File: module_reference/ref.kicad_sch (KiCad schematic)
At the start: 82 parts, among them J201 Conn_01x01, J202 Conn_01x01, J203 Conn_01x01, J204 Conn_01x01, J205 Conn_01x01, J206 Conn_01x01, J207 Conn_01x01, J208 Conn_01x01, Q201 BD135, U201 ADR1000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

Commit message: Rev 0.5 routed
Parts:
- R222, R224: now left out of the parts list
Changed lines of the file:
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@@
   )
   (symbol (lib_id "Device:R") (at 173.99 52.07 90) (unit 1)
-    (in_bom yes) (on_board yes) (fields_autoplaced)
+    (in_bom no) (on_board yes) (fields_autoplaced)
     (property "Reference" "R222" (id 0) (at 173.99 45.72 90))
     (property "Value" "DNP" (id 1) (at 173.99 48.26 90))
@@
   )
   (symbol (lib_id "Device:R") (at 173.99 102.87 90) (unit 1)
-    (in_bom yes) (on_board yes) (fields_autoplaced)
+    (in_bom no) (on_board yes) (fields_autoplaced)
     (property "Reference" "R224" (id 0) (at 173.99 96.52 90))
     (property "Value" "DNP" (id 1) (at 173.99 99.06 90))

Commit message: No longer configured for PRND by default
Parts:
- added J209, J210, J211, J212: Conn_01x01, Connector_Wire:SolderWire-0.1sqmm_1x01_D0.4mm_OD1mm, symbol Connector_Generic:Conn_01x01
- JP202, JP203, JP207, JP208, JP209, JP213, JP216, JP221: value Jumper_2_Bridged -> Jumper_2_Open; footprint Jumper:SolderJumper-2_P1.3mm_Bridged_RoundedPad1.0x1.5mm -> Jumper:SolderJumper-2_P1.3mm_Open_RoundedPad1.0x1.5mm; symbol Jumper:Jumper_2_Bridged -> Jumper:Jumper_2_Open
- JP204, JP205, JP206, JP210, JP211, JP217, JP219: value Jumper_2_Open -> Jumper_2_Bridged; footprint Jumper:SolderJumper-2_P1.3mm_Open_RoundedPad1.0x1.5mm -> Jumper:SolderJumper-2_P1.3mm_Bridged_RoundedPad1.0x1.5mm; symbol Jumper:Jumper_2_Open -> Jumper:Jumper_2_Bridged
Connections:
- net ADR_Pin6: now also J212.1 (Pin_1); no longer RN201.5 (R5.1)
- net ADR_Pin7: now also J209.1 (Pin_1)
- net RN201_Pin15: now also J210.1 (Pin_1)
- new net RN201_Pin5: J211.1 (Pin_1), RN201.5 (R5.1)
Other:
- moved on the sheet: J202, J204, J205, J207, JP203, JP204, JP205, JP206, JP209, JP210, JP216, JP217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

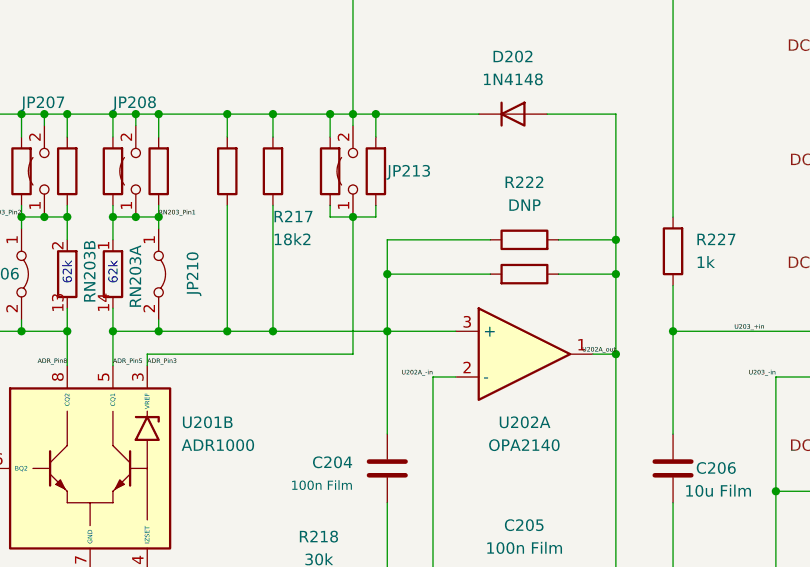
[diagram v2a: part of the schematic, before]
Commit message: New backplane, Reference Rev 0.6 with heated resistor network support
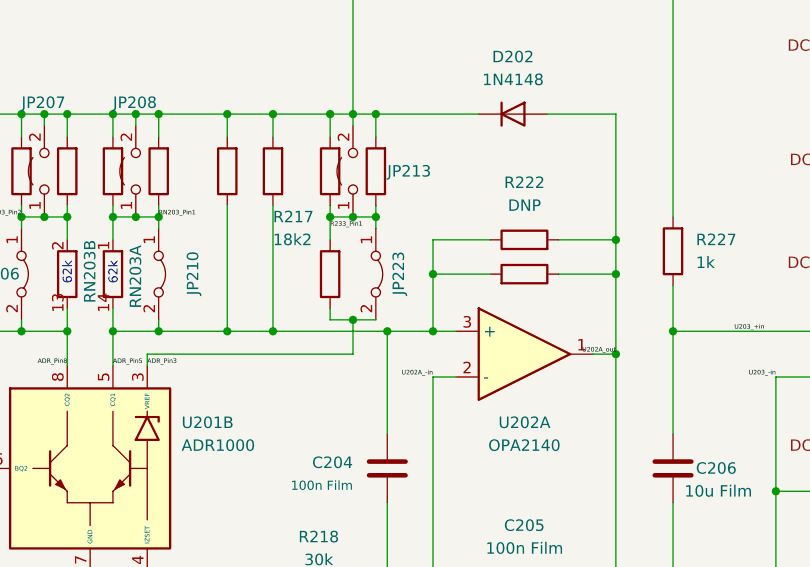
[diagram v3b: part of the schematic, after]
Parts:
- added JP223: Jumper_2_Bridged, Jumper:SolderJumper-2_P1.3mm_Bridged_RoundedPad1.0x1.5mm, symbol Jumper:Jumper_2_Bridged
- added R233: 0, Resistor_THT:R_Axial_DIN0204_L3.6mm_D1.6mm_P7.62mm_Horizontal, symbol Device:R
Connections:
- net ADR_Pin3: now also JP223.2 (B), R233.1; no longer JP213.1 (A), R219.1, R220.1
- new net R233_Pin1: JP213.1 (A), JP223.1 (A), R219.1, R220.1, R233.2
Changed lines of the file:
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@@
   (title_block
     (title "Reference and 10V buffer circuit")
-    (date "2022-05-23")
-    (rev "0.5")
+    (date "2022-08-15")
+    (rev "0.6")
     (company "RPG")
     (comment 1 "All resistors 0.1% MF unless otherwise noted")
@@
   (junction (at 71.12 179.07) (diameter 0) (color 0 0 0 0)
   )
+  (junction (at 163.83 62.23) (diameter 0) (color 0 0 0 0)
+  )
   (junction (at 71.12 191.77) (diameter 0) (color 0 0 0 0)
   )
@@
   (junction (at 241.3 133.35) (diameter 0) (color 0 0 0 0)
   )
-  (junction (at 158.75 55.88) (diameter 0) (color 0 0 0 0)
-  )
   (junction (at 265.43 147.32) (diameter 0) (color 0 0 0 0)
   )
@@
   (junction (at 62.23 179.07) (diameter 0) (color 0 0 0 0)
   )
+  (junction (at 152.4 49.53) (diameter 0) (color 0 0 0 0)
+  )
   (junction (at 163.83 102.87) (diameter 0) (color 0 0 0 0)
   )
@@
   (junction (at 176.53 143.51) (diameter 0) (color 0 0 0 0)
   )
+  (junction (at 157.48 49.53) (diameter 0) (color 0 0 0 0)
+  )
   (junction (at 140.97 62.23) (diameter 0) (color 0 0 0 0)
   )
@@
   (junction (at 233.68 90.17) (diameter 0) (color 0 0 0 0)
   )
+  (junction (at 163.83 55.88) (diameter 0) (color 0 0 0 0)
+  )
   (junction (at 201.93 102.87) (diameter 0) (color 0 0 0 0)
   )
@@
   (junction (at 129.54 114.3) (diameter 0) (color 0 0 0 0)
   )
+  (junction (at 154.94 60.96) (diameter 0) (color 0 0 0 0)
+  )
   (junction (at 232.41 133.35) (diameter 0) (color 0 0 0 0)
   )
@@
   (no_connect (at 223.52 72.39))
   (no_connect (at 220.98 72.39))
+  (wire (pts (xy 157.48 50.8) (xy 157.48 49.53))
+    (stroke (width 0) (type default) (color 0 0 0 0))
+  )
   (wire (pts (xy 218.44 72.39) (xy 218.44 74.93))
     (stroke (width 0) (type default) (color 0 0 0 0))
@@
     (stroke (width 0) (type default) (color 0 0 0 0))
   )
-  (wire (pts (xy 158.75 62.23) (xy 166.37 62.23))
-    (stroke (width 0) (type default) (color 0 0 0 0))
-  )
   (wire (pts (xy 154.94 91.44) (xy 163.83 91.44))
     (stroke (width 0) (type default) (color 0 0 0 0))
@@
     (stroke (width 0) (type default) (color 0 0 0 0))
   )
-  (wire (pts (xy 158.75 55.88) (xy 170.18 55.88))
-    (stroke (width 0) (type default) (color 0 0 0 0))
-  )
   (wire (pts (xy 231.14 64.77) (xy 238.76 64.77))
     (stroke (width 0) (type default) (color 0 0 0 0))
@@
     (stroke (width 0) (type default) (color 0 0 0 0))
   )
+  (wire (pts (xy 163.83 55.88) (xy 170.18 55.88))
+    (stroke (width 0) (type default) (color 0 0 0 0))
+  )
   (wire (pts (xy 93.98 62.23) (xy 118.11 62.23))
     (stroke (width 0) (type default) (color 0 0 0 0))
@@
     (stroke (width 0) (type default) (color 0 0 0 0))
   )
+  (wire (pts (xy 163.83 62.23) (xy 166.37 62.23))
+    (stroke (width 0) (type default) (color 0 0 0 0))
+  )
   (wire (pts (xy 177.8 106.68) (xy 184.15 106.68))
     (stroke (width 0) (type default) (color 0 0 0 0))
@@
     (stroke (width 0) (type default) (color 0 0 0 0))
   )
+  (wire (pts (xy 157.48 60.96) (xy 154.94 60.96))
+    (stroke (width 0) (type default) (color 0 0 0 0))
+  )
   (wire (pts (xy 265.43 133.35) (xy 274.32 133.35))
     (stroke (width 0) (type default) (color 0 0 0 0))
@@
     (stroke (width 0) (type default) (color 0 0 0 0))
   )
-  (wire (pts (xy 158.75 55.88) (xy 158.75 52.07))
+  (wire (pts (xy 163.83 55.88) (xy 163.83 52.07))
+    (stroke (width 0) (type default) (color 0 0 0 0))
+  )
+  (wire (pts (xy 154.94 60.96) (xy 152.4 60.96))
     (stroke (width 0) (type default) (color 0 0 0 0))
   )
@@
     (stroke (width 0) (type default) (color 0 0 0 0))
   )
+  (wire (pts (xy 154.94 64.77) (xy 154.94 60.96))
+    (stroke (width 0) (type default) (color 0 0 0 0))
+  )
   (wire (pts (xy 138.43 153.67) (xy 138.43 158.75))
     (stroke (width 0) (type default) (color 0 0 0 0))
@@
     (stroke (width 0) (type default) (color 0 0 0 0))
   )
+  (wire (pts (xy 152.4 60.96) (xy 152.4 59.69))
+    (stroke (width 0) (type default) (color 0 0 0 0))
+  )
   (wire (pts (xy 40.64 154.94) (xy 45.72 154.94))
     (stroke (width 0) (type default) (color 0 0 0 0))
@@
     (stroke (width 0) (type default) (color 0 0 0 0))
   )
+  (wire (pts (xy 152.4 52.07) (xy 152.4 49.53))
+    (stroke (width 0) (type default) (color 0 0 0 0))
+  )
   (wire (pts (xy 118.11 62.23) (xy 123.19 62.23))
     (stroke (width 0) (type default) (color 0 0 0 0))
@@
     (stroke (width 0) (type default) (color 0 0 0 0))
   )
-  (wire (pts (xy 158.75 62.23) (xy 158.75 55.88))
+  (wire (pts (xy 163.83 62.23) (xy 163.83 55.88))
     (stroke (width 0) (type default) (color 0 0 0 0))
   )
@@
     (stroke (width 0) (type default) (color 0 0 0 0))
   )
+  (wire (pts (xy 158.75 62.23) (xy 163.83 62.23))
+    (stroke (width 0) (type default) (color 0 0 0 0))
+  )
   (wire (pts (xy 120.65 38.1) (xy 123.19 38.1))
     (stroke (width 0) (type default) (color 0 0 0 0))
@@
     (stroke (width 0) (type default) (color 0 0 0 0))
   )
-  (wire (pts (xy 154.94 49.53) (xy 154.94 64.77))
-    (stroke (width 0) (type default) (color 0 0 0 0))
-  )
   (wire (pts (xy 85.09 53.34) (xy 93.98 53.34))
     (stroke (width 0) (type default) (color 0 0 0 0))
@@
     (stroke (width 0) (type default) (color 0 0 0 0))
   )
-  (wire (pts (xy 158.75 52.07) (xy 170.18 52.07))
+  (wire (pts (xy 163.83 52.07) (xy 170.18 52.07))
     (stroke (width 0) (type default) (color 0 0 0 0))
   )
@@
     (effects (font (size 1.27 1.27)) (justify left bottom))
   )
+  (label "R233_Pin1" (at 152.4 50.8 0)
+    (effects (font (size 0.5 0.5)) (justify left bottom))
+  )
   (label "RN201_Pin5" (at 54.61 154.94 0)
     (effects (font (size 0.635 0.635)) (justify left bottom))
@@
     (pin "2")
   )
-  (symbol (lib_id "ADRmu_Library:322146") (at 105.41 96.52 180) (unit 4)
+  (symbol (lib_name "322146_4") (lib_id "ADRmu_Library:322146") (at 105.41 96.52 180) (unit 4)
     (in_bom yes) (on_board yes)
     (property "Reference" "RN203" (id 0) (at 102.87 100.33 90)
@@
     (pin "2")
   )
+  (symbol (lib_id "Device:R") (at 152.4 55.88 180) (unit 1)
+    (in_bom no) (on_board yes) (fields_autoplaced)
+    (property "Reference" "R233" (id 0) (at 154.94 54.6099 0)
+      (effects (font (size 1.27 1.27)) (justify right) hide)
+    )
+    (property "Value" "0" (id 1) (at 154.94 57.1499 0)
+      (effects (font (size 1.27 1.27)) (justify right) hide)
+    )
+    (property "Footprint" "Resistor_THT:R_Axial_DIN0204_L3.6mm_D1.6mm_P7.62mm_Horizontal" (id 2) (at 154.178 55.88 90)
+      (effects (font (size 1.27 1.27)) hide)
+    )
+    (property "Datasheet" "~" (id 3) (at 152.4 55.88 0)
+      (effects (font (size 1.27 1.27)) hide)
+    )
+    (pin "1")
+    (pin "2")
+  )
   (symbol (lib_id "Jumper:Jumper_2_Open") (at 201.93 107.95 270) (unit 1)
     (in_bom no) (on_board yes)
@@
     (pin "3")
   )
-  (symbol (lib_id "ADRmu_Library:322146") (at 128.27 55.88 0) (unit 1)
+  (symbol (lib_name "322146_1") (lib_id "ADRmu_Library:322146") (at 128.27 55.88 0) (unit 1)
     (in_bom yes) (on_board yes)
     (property "Reference" "RN203" (id 0) (at 130.81 59.69 90)
@@
     (pin "2")
   )
-  (symbol (lib_id "ADRmu_Library:322146") (at 123.19 55.88 0) (unit 2)
+  (symbol (lib_name "322146_2") (lib_id "ADRmu_Library:322146") (at 123.19 55.88 0) (unit 2)
     (in_bom yes) (on_board yes)
     (property "Reference" "RN203" (id 0) (at 125.73 52.07 90)
@@
     (pin "2")
   )
-  (symbol (lib_id "ADRmu_Library:322146") (at 129.54 96.52 180) (unit 3)
+  (symbol (lib_name "322146_5") (lib_id "ADRmu_Library:322146") (at 129.54 96.52 180) (unit 3)
     (in_bom yes) (on_board yes)
     (property "Reference" "RN203" (id 0) (at 127 100.33 90)
@@
     (pin "2")
   )
-  (symbol (lib_id "ADRmu_Library:322146") (at 105.41 71.12 0) (unit 5)
+  (symbol (lib_name "322146_3") (lib_id "ADRmu_Library:322146") (at 105.41 71.12 0) (unit 5)
     (in_bom yes) (on_board yes)
     (property "Reference" "RN203" (id 0) (at 102.87 71.12 0)
@@
     (pin "2")
   )
-  (symbol (lib_id "ADRmu_Library:322146") (at 217.17 87.63 270) (unit 6)
+  (symbol (lib_name "322146_6") (lib_id "ADRmu_Library:322146") (at 217.17 87.63 270) (unit 6)
     (in_bom yes) (on_board yes)
     (property "Reference" "RN203" (id 0) (at 217.17 85.09 90))
@@
     (pin "9")
   )
+  (symbol (lib_id "Jumper:Jumper_2_Bridged") (at 157.48 55.88 270) (unit 1)
+    (in_bom no) (on_board yes)
+    (property "Reference" "JP223" (id 0) (at 160.02 53.34 0)
+      (effects (font (size 1.27 1.27)) (justify left))
+    )
+    (property "Value" "Jumper_2_Bridged" (id 1) (at 154.94 55.88 0)
+      (effects (font (size 1.27 1.27)) hide)
+    )
+    (property "Footprint" "Jumper:SolderJumper-2_P1.3mm_Bridged_RoundedPad1.0x1.5mm" (id 2) (at 157.48 55.88 0)
+      (effects (font (size 1.27 1.27)) hide)
+    )
+    (property "Datasheet" "~" (id 3) (at 157.48 55.88 0)
+      (effects (font (size 1.27 1.27)) hide)
+    )
+    (pin "1")
+    (pin "2")
+  )
   (symbol (lib_id "Device:R") (at 171.45 137.16 0) (mirror x) (unit 1)

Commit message: Ref module Rev. 0.9
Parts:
- removed C206: 10u Film, Capacitor_THT:C_Rect_L7.2mm_W11.0mm_P5.00mm_FKS2_FKP2_MKS2_MKP2, symbol Device:C
- removed C207: 100n 50V, Capacitor_SMD:C_0805_2012Metric, symbol Device:C
- removed C208: 220n Film, Capacitor_THT:C_Rect_L7.2mm_W3.0mm_P5.00mm_FKS2_FKP2_MKS2_MKP2, symbol Device:C
- removed C209: 1u Film, Capacitor_THT:C_Rect_L4.6mm_W5.5mm_P2.50mm_MKS02_FKP02, symbol Device:C
- removed JP212, JP214, JP215, JP216, JP221: Jumper_2_Open, Jumper:SolderJumper-2_P1.3mm_Open_RoundedPad1.0x1.5mm, symbol Jumper:Jumper_2_Open
- removed JP217, JP219: Jumper_2_Bridged, Jumper:SolderJumper-2_P1.3mm_Bridged_RoundedPad1.0x1.5mm, symbol Jumper:Jumper_2_Bridged
- removed R228, R231: 0, Crystal:Crystal_HC52-U_Vertical, symbol Device:R
- removed R229, R230: 0, Resistor_SMD:R_0805_2012Metric, symbol Device:R
- removed R232: 100, Resistor_SMD:R_0805_2012Metric, symbol Device:R
- removed R233: 0, Resistor_THT:R_Axial_DIN0204_L3.6mm_D1.6mm_P7.62mm_Horizontal, symbol Device:R
- removed RN202: Vishay TDP 10k, Package_DIP:DIP-16_W7.62mm, symbol ADRmu_Library:Vishay TDP
- removed RN203: 322146, Package_DIP:DIP-14_W7.62mm, symbol ADRmu_Library:322146
- removed U203: ADA4523-1, Package_SO:SOIC-8_3.9x4.9mm_P1.27mm, symbol ADRmu_Library:ADA4523-1
- added J214, J215, J216, J217: Conn_01x01, Connector_Wire:SolderWire-0.1sqmm_1x01_D0.4mm_OD1mm, symbol Connector_Generic:Conn_01x01
- added JPB201, JPH201: Jumper_2_Open, Jumper:SolderJumper-2_P1.3mm_Open_RoundedPad1.0x1.5mm, symbol Jumper:Jumper_2_Open
- added R234: 10k, Resistor_SMD:R_0805_2012Metric, symbol Device:R
- added RN203: 322146+1, ADRmu_Library:VPG322146+1, symbol ADRmu_Library:322146+1
- added TP201: TestPoint, TestPoint:TestPoint_THTPad_2.0x2.0mm_Drill1.0mm, symbol Connector:TestPoint
- C201, C202, C203: footprint Capacitor_SMD:C_0805_2012Metric -> Capacitor_SMD:C_0603_1608Metric
- C204, C205: value 100n Film -> 100n 50V; footprint Capacitor_THT:C_Rect_L7.2mm_W2.5mm_P5.00mm_FKS2_FKP2_MKS2_MKP2 -> Capacitor_SMD:C_0603_1608Metric
- J201, J202, J203, J204, J205, J206, J207, J208, J209, J210, J211, J212: now left out of the parts list
- R216, R217: value 18k2 -> DNP
- R221: footprint Crystal:Crystal_HC52-U_Vertical -> Resistor_SMD:R_0805_2012Metric; now in the parts list
- R222, R223, R224, R225, R226: value DNP -> TBD
- R227: value 1k -> TBD; now left out of the parts list
- U202: value OPA2140 -> OPA2172
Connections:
- net U203_+in is gone; now on net U202A_-in: R227.1
- net 7Vref: now also R221.1, J214.1 (Pin_1); no longer R227.2
- net ADR_Pin3: now also RN203.8 (1.1)
- net ADR_Pin4: now also RN203.12 (R3.2)
- net ADR_Pin5: now also R226.1, RN203.14 (1.2)
- net ADR_Pin6: now also J217.1 (Pin_1), R234.2, RN203.11 (R4.2), RN203.11 (R5.2); no longer J212.1 (Pin_1), RN201.6 (R6.1)
- net ADR_Pin7: now also J215.1 (Pin_1), J216.1 (Pin_1), JPB201.2 (B); no longer J209.1 (Pin_1), RN201.10 (R7.2)
- net ADR_Pin8: now also RN203.13 (R2.2)
- net Q201_base: now also TP201.1
- net RN203_Pin1: now also RN203.1 (1.1)
- net RN203_Pin2: now also RN203.2 (R2.1)
- net RN203_Pin3: now also RN203.3 (R3.1)
- net RN203_Pin4: now also RN203.4 (R4.1)
- net RN203_Pin5: now also RN203.5 (R5.1)
- net U202A_out: now also R226.2, R227.2
- net DC_DC_GND renamed GNDf
- net GNDf: now also JPH201.2 (B); no longer D201.1 (K)
- net DC_DC_Vin+ renamed 12Vf
- net 12Vf: now also R221.2
- removed net JP214_Pin2: R221.1, R226.1
- net R206_Pin1 renamed R204_Pin1
- net R233_Pin1 renamed J213_Pin1
- net J213_Pin1: now also RN203.9 (8..2)
- removed net RN202_Pin9: R221.2, R226.2
- new net JPB_Pin1: JPB201.1 (A), R234.1
- new net JPH_Pin1: D201.1 (K), JPH201.1 (A)
- new net RN201_Pin10: J209.1 (Pin_1), RN201.10 (R7.2)
- new net RN201_Pin6: J212.1 (Pin_1), RN201.6 (R6.1)
- no-connect marks 2 -> 0
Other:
- note removed: "10k"
- note removed: "13k"
- note removed: "1k"
- note removed: "20k"
- note removed: "62k"
- note removed: "95R"
- title: Reference and 10V buffer circuit -> Reference circuit
- moved on the sheet: C201, C202, C203, C204, D201, D202, J203, J208, J209, J212, JP201, JP202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

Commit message: asdf
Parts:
- removed JP213: Jumper_2_Open, Jumper:SolderJumper-2_P1.3mm_Open_RoundedPad1.0x1.5mm, symbol Jumper:Jumper_2_Open
- added JP213: Jumper_2_Bridged, Jumper:SolderJumper-2_P1.3mm_Bridged_RoundedPad1.0x1.5mm, symbol Jumper:Jumper_2_Bridged
- R210: value 0 -> 62k; now in the parts list
- R221: now left out of the parts list
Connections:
- net 7Vref: now also JP213.1 (A)
- net J213_Pin1: now also JP213.2 (B)
